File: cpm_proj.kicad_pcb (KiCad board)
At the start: 2 copper layers, 100 x 100 mm, 95 parts, among them J11 USB_C_Receptacle_USB2.0, SW1 RESET, U1 Sparkfun Artemis, U2 ADP5091, U3 RFM95W-915S2, U4 TPS22860, U5 LD1117AV33_TO220, U6 TPS22860, Y1 32.768kHz

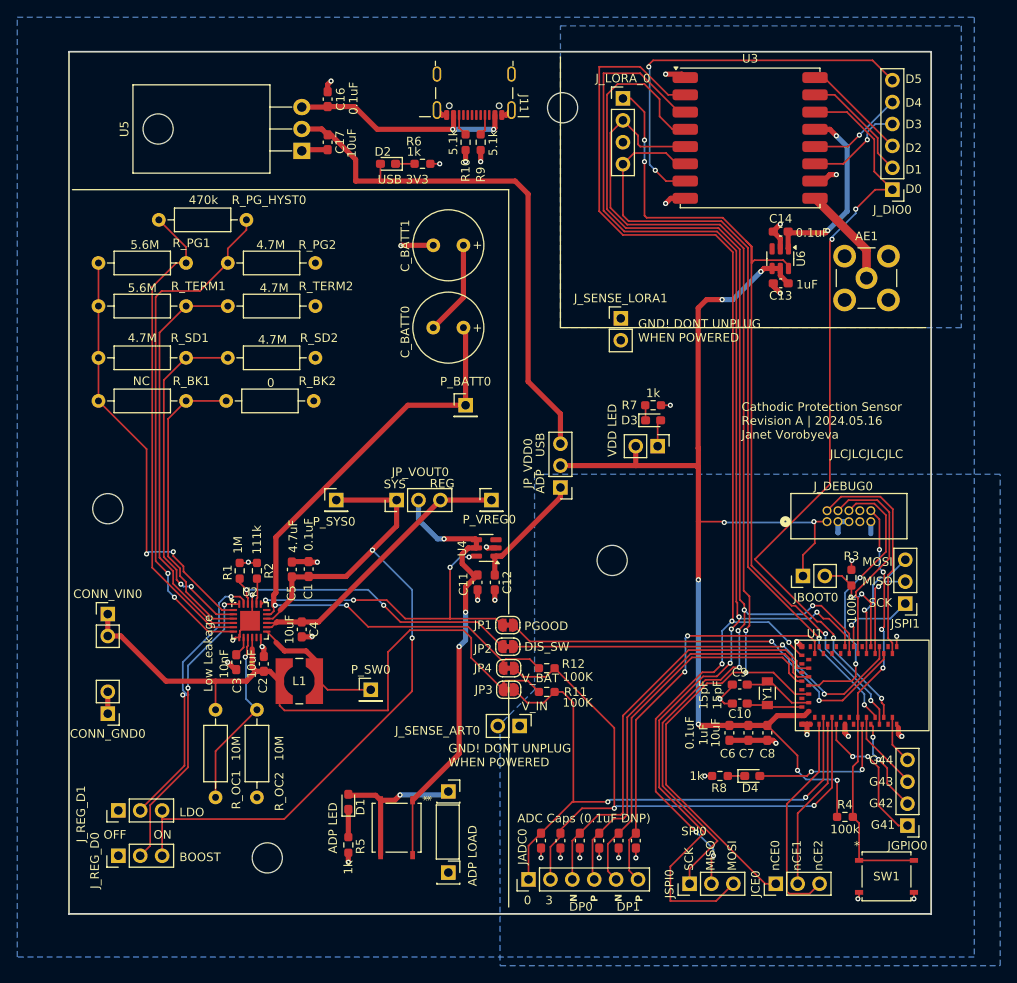
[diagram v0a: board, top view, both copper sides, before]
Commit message: Revision B
Fixed SWDIO/SWDCK
Relabeled ADC Caps to 10nF
Relabelled LORA reset line to active low
Minor silkscreen tweaks
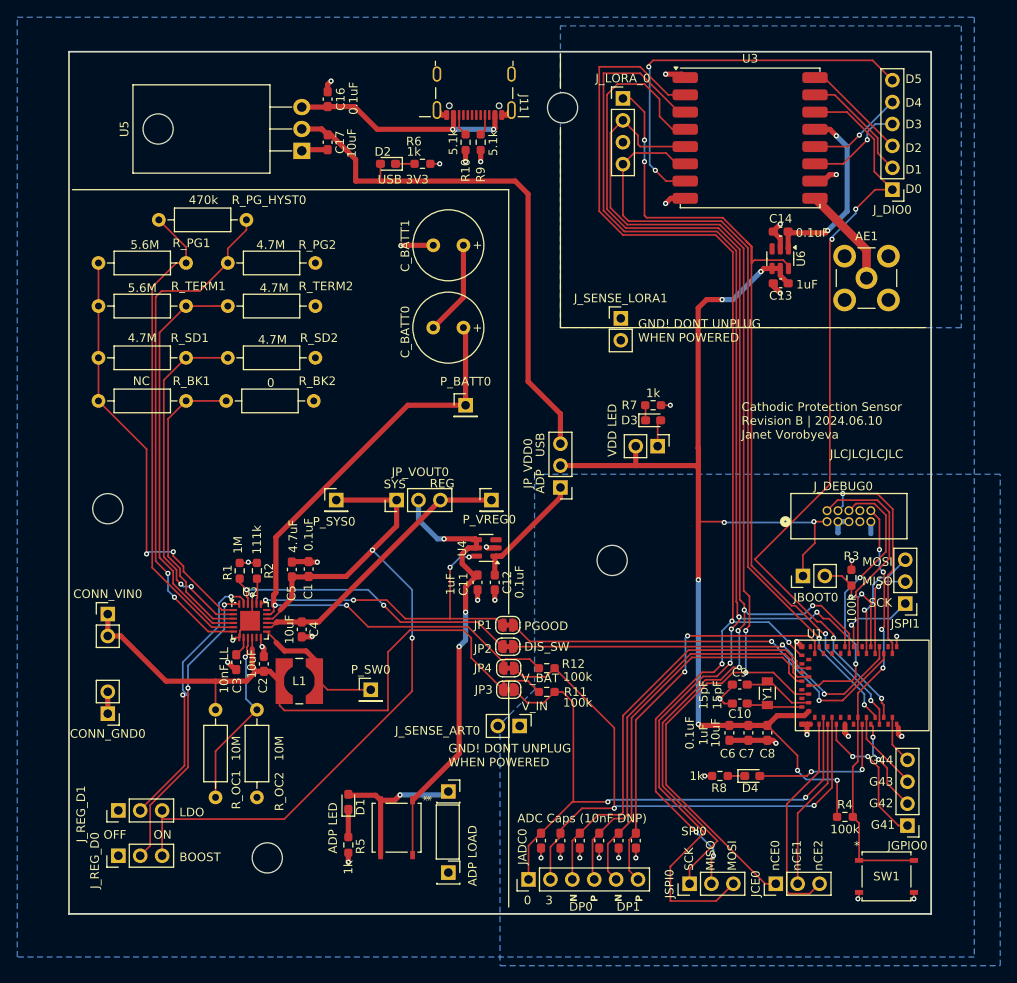
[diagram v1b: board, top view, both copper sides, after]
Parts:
- C3: value 10nF -> 10nF LL
- H1, H2, H3, H4: renamed from REF**; value MountingHole_3.5mm -> MountingHole
- R11, R12: value 100K -> 100k
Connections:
- net /artemis/LORA_RST renamed /artemis/LORA_nRST
- J_DEBUG0 pad 2: /artemis/SWDCK -> /artemis/SWDIO
- J_DEBUG0 pad 4: /artemis/SWDIO -> /artemis/SWDCK
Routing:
- net /artemis/SWDIO: track 25.1 -> 26.4 mm
- net /artemis/SWDCK: track 26.1 -> 25.9 mm, vias 0 -> 1
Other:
- board text added: "ADC Caps (10nF DNP)"
- board text added: "Cathodic Protection Sensor Revision B | 2024.06.10 Janet Vorobyeva"
- board text removed: "ADC Caps (0.1uF DNP)"
- board text removed: "Cathodic Protection Sensor Revision A | 2024.05.16 Janet Vorobyeva"
- board text removed: "Low Leakage"
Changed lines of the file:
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@@
 	(net 92 "unconnected-(J11-D--PadA7)")
 	(net 93 "unconnected-(J11-D--PadB7)")
-	(net 94 "/artemis/LORA_RST")
+	(net 94 "/artemis/LORA_nRST")
 	(net 95 "Net-(J_DIO0-Pin_3)")
 	(net 96 "Net-(J_DIO0-Pin_4)")
@@
 		(descr "Mounting Hole 3.5mm, no annular")
 		(tags "mounting hole 3.5mm no annular")
-		(property "Reference" "REF**"
+		(property "Reference" "H2"
 			(at 0 -4.5 0)
 			(layer "F.SilkS")
@@
 			)
 		)
-		(property "Value" "MountingHole_3.5mm"
+		(property "Value" "MountingHole"
 			(at 0 4.5 0)
 			(layer "F.Fab")
@@
 			)
 		)
-		(property "Description" ""
+		(property "Description" "Mounting Hole without connection"
 			(at 0 0 0)
 			(unlocked yes)
@@
 			)
 		)
+		(property ki_fp_filters "MountingHole*")
+		(sheetname "Root")
+		(sheetfile "cpm_proj.kicad_sch")
 		(attr exclude_from_pos_files exclude_from_bom)
 		(fp_circle
@@
 			(layers "F.Cu" "F.Paste" "F.Mask")
 			(roundrect_rratio 0.25)
-			(net 94 "/artemis/LORA_RST")
-			(pinfunction "RESET")
+			(net 94 "/artemis/LORA_nRST")
+			(pinfunction "nRESET")
 			(pintype "bidirectional")
 		)
@@
 		(descr "Mounting Hole 3.5mm, no annular")
 		(tags "mounting hole 3.5mm no annular")
-		(property "Reference" "REF**"
+		(property "Reference" "H1"
 			(at 0 -4.5 0)
 			(layer "F.SilkS")
@@
 			)
 		)
-		(property "Value" "MountingHole_3.5mm"
+		(property "Value" "MountingHole"
 			(at 0 4.5 0)
 			(layer "F.Fab")
@@
 			)
 		)
-		(property "Description" ""
+		(property "Description" "Mounting Hole without connection"
 			(at 0 0 0)
 			(unlocked yes)
@@
 			)
 		)
+		(property ki_fp_filters "MountingHole*")
+		(sheetname "Root")
+		(sheetfile "cpm_proj.kicad_sch")
 		(attr exclude_from_pos_files exclude_from_bom)
 		(fp_circle
@@
 			)
 		)
-		(property "Value" "10nF"
-			(at -0.2 -1.4 90)
+		(property "Value" "10nF LL"
+			(at -0.95 -1.4 90)
 			(layer "F.SilkS")
 			(effects
@@
 			)
 		)
-		(property "Datasheet" ""
+		(property "Datasheet" "https://www.digikey.com/en/products/detail/murata-electronics/GRT1885C1E103JA02J/13904823"
 			(at 0 0 90)
 			(unlocked yes)
@@
 			)
 		)
-		(property "Description" "Unpolarized capacitor, small symbol"
+		(property "Description" "Must be low leakage capacitor for MPPT tracking"
 			(at 0 0 90)
 			(unlocked yes)
@@
 			)
 		)
+		(property "PN" "GRT1885C1E103JA02J"
+			(at 0 0 90)
+			(unlocked yes)
+			(layer "F.Fab")
+			(hide yes)
+			(effects
+				(font
+					(size 1 1)
+					(thickness 0.15)
+				)
+			)
+		)
+		(property "Digikey PN" "490-GRT1885C1E103JA02JCT-ND"
+			(at 0 0 90)
+			(unlocked yes)
+			(layer "F.Fab")
+			(hide yes)
+			(effects
+				(font
+					(size 1 1)
+					(thickness 0.15)
+				)
+			)
+		)
 		(property ki_fp_filters "C_*")
 		(sheetname "power")
@@
 		(descr "Mounting Hole 3.5mm, no annular")
 		(tags "mounting hole 3.5mm no annular")
-		(property "Reference" "REF**"
+		(property "Reference" "H4"
 			(at 0 -4.5 0)
 			(layer "F.SilkS")
@@
 			)
 		)
-		(property "Value" "MountingHole_3.5mm"
+		(property "Value" "MountingHole"
 			(at 0 4.5 0)
 			(layer "F.Fab")
@@
 			)
 		)
-		(property "Description" ""
+		(property "Description" "Mounting Hole without connection"
 			(at 0 0 0)
 			(unlocked yes)
@@
 			)
 		)
+		(property ki_fp_filters "MountingHole*")
+		(sheetname "Root")
+		(sheetfile "cpm_proj.kicad_sch")
 		(attr exclude_from_pos_files exclude_from_bom)
 		(fp_circle
@@
 			)
 		)
-		(property "Value" "100K"
+		(property "Value" "100k"
 			(at 3.5875 1 0)
 			(layer "F.SilkS")
@@
 		(descr "Mounting Hole 3.5mm, no annular")
 		(tags "mounting hole 3.5mm no annular")
-		(property "Reference" "REF**"
+		(property "Reference" "H3"
 			(at 0 -4.5 0)
 			(layer "F.SilkS")
@@
 			)
 		)
-		(property "Value" "MountingHole_3.5mm"
+		(property "Value" "MountingHole"
 			(at 0 4.5 0)
 			(layer "F.Fab")
@@
 			)
 		)
-		(property "Description" ""
+		(property "Description" "Mounting Hole without connection"
 			(at 0 0 0)
 			(unlocked yes)
@@
 			)
 		)
+		(property ki_fp_filters "MountingHole*")
+		(sheetname "Root")
+		(sheetfile "cpm_proj.kicad_sch")
 		(attr exclude_from_pos_files exclude_from_bom)
 		(fp_circle
@@
 			(layers "*.Cu" "*.Mask")
 			(remove_unused_layers no)
-			(net 56 "/artemis/SWDCK")
+			(net 64 "/artemis/SWDIO")
 			(pinfunction "Pin_2")
 			(pintype "passive")
@@
 			(layers "*.Cu" "*.Mask")
 			(remove_unused_layers no)
-			(net 64 "/artemis/SWDIO")
+			(net 56 "/artemis/SWDCK")
 			(pinfunction "Pin_4")
 			(pintype "passive")
@@
 			)
 		)
-		(property "Value" "100K"
+		(property "Value" "100k"
 			(at 3.5875 1.25 0)
 			(layer "F.SilkS")
@@
 			(size 0.4 0.6)
 			(layers "F.Cu" "F.Paste" "F.Mask")
-			(net 94 "/artemis/LORA_RST")
+			(net 94 "/artemis/LORA_nRST")
 			(pinfunction "GPIO3")
 			(pintype "bidirectional")
@@
 		)
 		(property "Value" "0.1uF"
-			(at 0 1.43 90)
-			(layer "F.Fab")
+			(at -0.05 -2.8625 90)
+			(layer "F.SilkS")
 			(effects
 				(font
@@
 			(layers "*.Cu" "*.Mask")
 			(remove_unused_layers no)
-			(net 94 "/artemis/LORA_RST")
+			(net 94 "/artemis/LORA_nRST")
 			(pinfunction "Pin_4")
 			(pintype "passive")
@@
 		)
 		(property "Value" "1uF"
-			(at 0 1.43 90)
-			(layer "F.Fab")
+			(at 0.2 3.1375 90)
+			(layer "F.SilkS")
 			(effects
 				(font
@@
 	)
 	(gr_line
+		(start 119 45.25)
+		(end 119 41.25)
+		(stroke
+			(width 0.1)
+			(type default)
+		)
+		(layer "F.SilkS")
+	)
+	(gr_line
 		(start 113 106.2)
 		(end 113 57)
@@
 	)
 	(gr_line
-		(start 119 41.6)
+		(start 119 49.75)
 		(end 119 73)
 		(stroke
@@
 		)
 	)
-	(gr_text "Cathodic Protection Sensor\nRevision A | 2024.05.16\nJanet Vorobyeva"
+	(gr_text "Cathodic Protection Sensor\nRevision B | 2024.06.10\nJanet Vorobyeva"
 		(at 140 86 0)
 		(layer "F.SilkS")
@@
 		)
 	)
-	(gr_text "ADC Caps (0.1uF DNP)"
+	(gr_text "ADC Caps (10nF DNP)"
 		(at 114 130.5 0)
 		(layer "F.SilkS")
@@
 		)
 	)
-	(gr_text "Low Leakage"
-		(at 78.75 115.25 90)
-		(layer "F.SilkS")
-		(effects
-			(font
-				(size 1 1)
-				(thickness 0.16)
-			)
-			(justify left bottom)
-		)
-	)
 	(gr_text "JLCJLCJLCJLC"
 		(at 181 54.75 0)
@@
 	)
 	(segment
+		(start 156.105 92.605)
+		(end 155.75 92.25)
+		(width 0.2)
+		(layer "F.Cu")
+		(net 56)
+	)
+	(segment
 		(start 157 101.711696)
 		(end 157 109.048529)
@@
 	)
 	(segment
-		(start 151.545 92.605)
-		(end 156.105 92.605)
+		(start 157.55 101.161696)
+		(end 157 101.711696)
 		(width 0.2)
 		(layer "F.Cu")
@@
 	)
 	(segment
-		(start 157.55 101.161696)
-		(end 157 101.711696)
+		(start 155.75 92.25)
+		(end 151.75 92.25)
 		(width 0.2)
 		(layer "F.Cu")
 		(net 56)
 	)
+	(via
+		(at 151.75 92.25)
+		(size 0.6)
+		(drill 0.3)
+		(layers "F.Cu" "B.Cu")
+		(net 56)
+	)
 	(segment
-		(start 149.92 94.23)
-		(end 151.545 92.605)
+		(start 151.75 92.25)
+		(end 151.75 93.67)
 		(width 0.2)
-		(layer "F.Cu")
+		(layer "B.Cu")
 		(net 56)
 	)
 	(segment
-		(start 152.415 93.005)
-		(end 155.755 93.005)
+		(start 151.75 93.67)
+		(end 151.19 94.23)
+		(width 0.2)
+		(layer "B.Cu")
+		(net 56)
+	)
+	(segment
+		(start 153.5 104.359737)
+		(end 153.291131 104.150868)
 		(width 0.2)
 		(layer "F.Cu")
@@
 	)
 	(segment
-		(start 157.15 94.4)
-		(end 157.15 99.766722)
+		(start 157.15 99.766722)
+		(end 157.15 94.4)
 		(width 0.2)
 		(layer "F.Cu")
@@
 	)
 	(segment
-		(start 153.291131 103.625591)
-		(end 153.291131 104.150868)
+		(start 155.755 93.005)
+		(end 151.145 93.005)
 		(width 0.2)
 		(layer "F.Cu")
@@
 	)
 	(segment
-		(start 151.19 94.23)
-		(end 152.415 93.005)
+		(start 153.291131 103.625591)
+		(end 157.15 99.766722)
 		(width 0.2)
 		(layer "F.Cu")
@@
 	)
 	(segment
-		(start 153.5 104.359737)
-		(end 153.5 110.8)
+		(start 153.5 110.8)
+		(end 153.5 104.359737)
 		(width 0.2)
 		(layer "F.Cu")
@@
 	)
 	(segment
-		(start 155.755 93.005)
-		(end 157.15 94.4)
+		(start 153.291131 104.150868)
+		(end 153.291131 103.625591)
 		(width 0.2)
 		(layer "F.Cu")
@@
 	)
 	(segment
-		(start 157.15 99.766722)
-		(end 153.291131 103.625591)
+		(start 157.15 94.4)
+		(end 155.755 93.005)
 		(width 0.2)
 		(layer "F.Cu")
@@
 	)
 	(segment
-		(start 153.291131 104.150868)
-		(end 153.5 104.359737)
+		(start 151.145 93.005)
+		(end 149.92 94.23)
 		(width 0.2)
 		(layer "F.Cu")
